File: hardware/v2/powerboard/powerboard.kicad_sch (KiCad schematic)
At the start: 36 parts, among them J1 LEG1_PWR, J10 UBEC3, J11 SBEC, J12 LOGIC_5V_OUT, J13 MONITOR, J2 LEG2_PWR, J3 LEG3_PWR, J4 LEG4_PWR, J5 LEG5_PWR, J6 LEG6_PWR, J7 BATTERY, J8 UBEC1, J9 UBEC2, Q1 IRF9540NPBF, Q2 IRF9540NPBF, Q3 MMBT3904, SW1 MASTER_SW

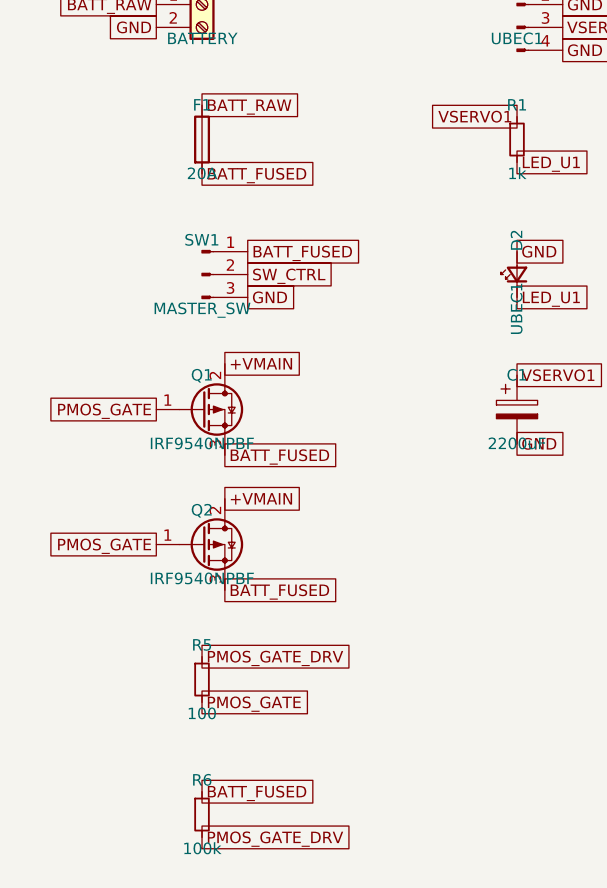
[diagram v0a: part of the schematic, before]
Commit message: hardware: replace F1 main fuse holder with soldered SMD fuse
TME stocks no SMD automotive blade-fuse holder, and the THT mini-blade
holder was awkward to hand-solder. Switch F1 to Schurter 3413.0331.22
(1206 SMD, 20A, time-lag), soldered directly with a stock KiCad
Fuse_1206_3216Metric footprint -- non-replaceable, but a blown fuse on
the main battery input means a fault needs tracing anyway.

Co-Authored-By: Claude Sonnet 5 <noreply@anthropic.com>
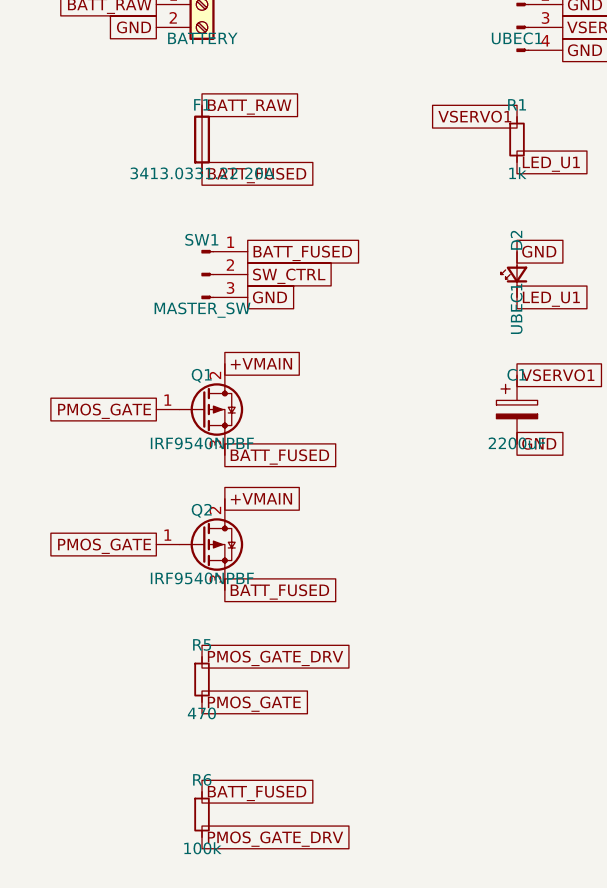
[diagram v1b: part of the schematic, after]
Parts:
- F1: value 20A -> 3413.0331.22 20A; footprint Custom:Fuse Holder Mini -> Fuse:Fuse_1206_3216Metric
- R5: value 100 -> 470
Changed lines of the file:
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@@
 			)
 		)
-		(property "Value" "20A"
+		(property "Value" "3413.0331.22 20A"
 			(at 35 53.81 0)
 			(effects
@@
 			)
 		)
-		(property "Footprint" "Custom:Fuse Holder Mini"
+		(property "Footprint" "Fuse:Fuse_1206_3216Metric"
 			(at 35 50 0)
 			(effects
@@
 			)
 		)
-		(property "Value" "100"
+		(property "Value" "470"
 			(at 35 113.81 0)
 			(effects
